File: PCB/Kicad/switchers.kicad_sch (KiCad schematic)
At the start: 44 parts, among them SW1 SWPADL1, SW10 SWPADR2, SW11 SWPADR3, SW12 SWPADR4, SW13 SWPADR5, SW14 SWPADR6, SW15 SWPADR7, SW16 SWPADR8, SW17 SWPLAYL, SW18 SWCUEL, SW19 SWSHIFTL, SW2 SWPADL2, SW20 SWSYNCL, SW21 SWRANGEL, SW22 SWFX1L, SW23 SWFX2L, SW24 SWFX3L, SW25 SWBR-PREVL, SW26 SWBR-BACKL, SW27 SWPLAYR, SW28 SWCUER, SW29 SWSHIFTR, SW3 SWPADL3, SW30 SWSYNCR, SW31 SWRANGER, SW32 SWFX1R, SW33 SWFX2R, SW34 SWFX3R, SW35 SWBR-PREVR, SW36 SWBR-BACKR, SW37 SWPCUEL1, SW38 SWPCUEL2, SW39 SWPCUEL3, SW4 SWPADL4, SW40 SWSEL1, SW41 SWSEL2, SW42 SWSEL3, SW43 BROWSER-L, SW44 BROWSER-R, SW5 SWPADL5, SW6 SWPADL6, SW7 SWPADL7, SW8 SWPADL8, SW9 SWPADR1

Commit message: fixing 3dmodels
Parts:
- SW17, SW18, SW19, SW20, SW21, SW22, SW23, SW24, SW25, SW26, SW27, SW28, SW29, SW30, SW31, SW32, SW33, SW34, SW35, SW36, SW37, SW38, SW39, SW40, SW41, SW42: footprint Button_Switch_THT:SW_PUSH_6mm_H5mm -> Library:SW_PUSH_6mm_H5mm
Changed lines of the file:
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@@
     (property "Reference" "SW17" (id 0) (at 106.68 25.781 0))
     (property "Value" "SWPLAYL" (id 1) (at 106.68 28.0924 0))
-    (property "Footprint" "Button_Switch_THT:SW_PUSH_6mm_H5mm" (id 2) (at 106.68 27.94 0)
+    (property "Footprint" "Library:SW_PUSH_6mm_H5mm" (id 2) (at 106.68 27.94 0)
       (effects (font (size 1.27 1.27)) hide)
     )
@@
     (property "Reference" "SW18" (id 0) (at 106.68 43.561 0))
     (property "Value" "SWCUEL" (id 1) (at 106.68 45.8724 0))
-    (property "Footprint" "Button_Switch_THT:SW_PUSH_6mm_H5mm" (id 2) (at 106.68 45.72 0)
+    (property "Footprint" "Library:SW_PUSH_6mm_H5mm" (id 2) (at 106.68 45.72 0)
       (effects (font (size 1.27 1.27)) hide)
     )
@@
     (property "Reference" "SW19" (id 0) (at 106.68 58.801 0))
     (property "Value" "SWSHIFTL" (id 1) (at 106.68 61.1124 0))
-    (property "Footprint" "Button_Switch_THT:SW_PUSH_6mm_H5mm" (id 2) (at 106.68 60.96 0)
+    (property "Footprint" "Library:SW_PUSH_6mm_H5mm" (id 2) (at 106.68 60.96 0)
       (effects (font (size 1.27 1.27)) hide)
     )
@@
     (property "Reference" "SW20" (id 0) (at 106.68 75.311 0))
     (property "Value" "SWSYNCL" (id 1) (at 106.68 77.6224 0))
-    (property "Footprint" "Button_Switch_THT:SW_PUSH_6mm_H5mm" (id 2) (at 106.68 77.47 0)
+    (property "Footprint" "Library:SW_PUSH_6mm_H5mm" (id 2) (at 106.68 77.47 0)
       (effects (font (size 1.27 1.27)) hide)
     )
@@
     (property "Reference" "SW21" (id 0) (at 106.68 90.551 0))
     (property "Value" "SWRANGEL" (id 1) (at 106.68 92.8624 0))
-    (property "Footprint" "Button_Switch_THT:SW_PUSH_6mm_H5mm" (id 2) (at 106.68 92.71 0)
+    (property "Footprint" "Library:SW_PUSH_6mm_H5mm" (id 2) (at 106.68 92.71 0)
       (effects (font (size 1.27 1.27)) hide)
     )
@@
     (property "Reference" "SW22" (id 0) (at 106.68 107.061 0))
     (property "Value" "SWFX1L" (id 1) (at 106.68 109.3724 0))
-    (property "Footprint" "Button_Switch_THT:SW_PUSH_6mm_H5mm" (id 2) (at 106.68 109.22 0)
+    (property "Footprint" "Library:SW_PUSH_6mm_H5mm" (id 2) (at 106.68 109.22 0)
       (effects (font (size 1.27 1.27)) hide)
     )
@@
     (property "Reference" "SW23" (id 0) (at 106.68 123.571 0))
     (property "Value" "SWFX2L" (id 1) (at 106.68 125.8824 0))
-    (property "Footprint" "Button_Switch_THT:SW_PUSH_6mm_H5mm" (id 2) (at 106.68 125.73 0)
+    (property "Footprint" "Library:SW_PUSH_6mm_H5mm" (id 2) (at 106.68 125.73 0)
       (effects (font (size 1.27 1.27)) hide)
     )
@@
     (property "Reference" "SW24" (id 0) (at 106.68 140.081 0))
     (property "Value" "SWFX3L" (id 1) (at 106.68 142.3924 0))
-    (property "Footprint" "Button_Switch_THT:SW_PUSH_6mm_H5mm" (id 2) (at 106.68 142.24 0)
+    (property "Footprint" "Library:SW_PUSH_6mm_H5mm" (id 2) (at 106.68 142.24 0)
       (effects (font (size 1.27 1.27)) hide)
     )
@@
     (property "Reference" "SW25" (id 0) (at 106.68 160.401 0))
     (property "Value" "SWBR-PREVL" (id 1) (at 106.68 162.7124 0))
-    (property "Footprint" "Button_Switch_THT:SW_PUSH_6mm_H5mm" (id 2) (at 106.68 162.56 0)
+    (property "Footprint" "Library:SW_PUSH_6mm_H5mm" (id 2) (at 106.68 162.56 0)
       (effects (font (size 1.27 1.27)) hide)
     )
@@
     (property "Reference" "SW26" (id 0) (at 106.68 178.181 0))
     (property "Value" "SWBR-BACKL" (id 1) (at 106.68 180.4924 0))
-    (property "Footprint" "Button_Switch_THT:SW_PUSH_6mm_H5mm" (id 2) (at 106.68 180.34 0)
+    (property "Footprint" "Library:SW_PUSH_6mm_H5mm" (id 2) (at 106.68 180.34 0)
       (effects (font (size 1.27 1.27)) hide)
     )
@@
     (property "Reference" "SW27" (id 0) (at 140.97 25.781 0))
     (property "Value" "SWPLAYR" (id 1) (at 140.97 28.0924 0))
-    (property "Footprint" "Button_Switch_THT:SW_PUSH_6mm_H5mm" (id 2) (at 140.97 27.94 0)
+    (property "Footprint" "Library:SW_PUSH_6mm_H5mm" (id 2) (at 140.97 27.94 0)
       (effects (font (size 1.27 1.27)) hide)
     )
@@
     (property "Reference" "SW28" (id 0) (at 140.97 43.561 0))
     (property "Value" "SWCUER" (id 1) (at 140.97 45.8724 0))
-    (property "Footprint" "Button_Switch_THT:SW_PUSH_6mm_H5mm" (id 2) (at 140.97 45.72 0)
+    (property "Footprint" "Library:SW_PUSH_6mm_H5mm" (id 2) (at 140.97 45.72 0)
       (effects (font (size 1.27 1.27)) hide)
     )
@@
     (property "Reference" "SW29" (id 0) (at 140.97 58.801 0))
     (property "Value" "SWSHIFTR" (id 1) (at 140.97 61.1124 0))
-    (property "Footprint" "Button_Switch_THT:SW_PUSH_6mm_H5mm" (id 2) (at 140.97 60.96 0)
+    (property "Footprint" "Library:SW_PUSH_6mm_H5mm" (id 2) (at 140.97 60.96 0)
       (effects (font (size 1.27 1.27)) hide)
     )
@@
     (property "Reference" "SW30" (id 0) (at 140.97 75.311 0))
     (property "Value" "SWSYNCR" (id 1) (at 140.97 77.6224 0))
-    (property "Footprint" "Button_Switch_THT:SW_PUSH_6mm_H5mm" (id 2) (at 140.97 77.47 0)
+    (property "Footprint" "Library:SW_PUSH_6mm_H5mm" (id 2) (at 140.97 77.47 0)
       (effects (font (size 1.27 1.27)) hide)
     )
@@
     (property "Reference" "SW31" (id 0) (at 140.97 90.551 0))
     (property "Value" "SWRANGER" (id 1) (at 140.97 92.8624 0))
-    (property "Footprint" "Button_Switch_THT:SW_PUSH_6mm_H5mm" (id 2) (at 140.97 92.71 0)
+    (property "Footprint" "Library:SW_PUSH_6mm_H5mm" (id 2) (at 140.97 92.71 0)
       (effects (font (size 1.27 1.27)) hide)
     )
@@
     (property "Reference" "SW32" (id 0) (at 140.97 107.061 0))
     (property "Value" "SWFX1R" (id 1) (at 140.97 109.3724 0))
-    (property "Footprint" "Button_Switch_THT:SW_PUSH_6mm_H5mm" (id 2) (at 140.97 109.22 0)
+    (property "Footprint" "Library:SW_PUSH_6mm_H5mm" (id 2) (at 140.97 109.22 0)
       (effects (font (size 1.27 1.27)) hide)
     )
@@
     (property "Reference" "SW33" (id 0) (at 140.97 123.571 0))
     (property "Value" "SWFX2R" (id 1) (at 140.97 125.8824 0))
-    (property "Footprint" "Button_Switch_THT:SW_PUSH_6mm_H5mm" (id 2) (at 140.97 125.73 0)
+    (property "Footprint" "Library:SW_PUSH_6mm_H5mm" (id 2) (at 140.97 125.73 0)
       (effects (font (size 1.27 1.27)) hide)
     )
@@
     (property "Reference" "SW34" (id 0) (at 140.97 140.081 0))
     (property "Value" "SWFX3R" (id 1) (at 140.97 142.3924 0))
-    (property "Footprint" "Button_Switch_THT:SW_PUSH_6mm_H5mm" (id 2) (at 140.97 142.24 0)
+    (property "Footprint" "Library:SW_PUSH_6mm_H5mm" (id 2) (at 140.97 142.24 0)
       (effects (font (size 1.27 1.27)) hide)
     )
@@
     (property "Reference" "SW35" (id 0) (at 143.51 160.401 0))
     (property "Value" "SWBR-PREVR" (id 1) (at 143.51 162.7124 0))
-    (property "Footprint" "Button_Switch_THT:SW_PUSH_6mm_H5mm" (id 2) (at 143.51 162.56 0)
+    (property "Footprint" "Library:SW_PUSH_6mm_H5mm" (id 2) (at 143.51 162.56 0)
       (effects (font (size 1.27 1.27)) hide)
     )
@@
     (property "Reference" "SW36" (id 0) (at 143.51 178.181 0))
     (property "Value" "SWBR-BACKR" (id 1) (at 143.51 180.4924 0))
-    (property "Footprint" "Button_Switch_THT:SW_PUSH_6mm_H5mm" (id 2) (at 143.51 180.34 0)
+    (property "Footprint" "Library:SW_PUSH_6mm_H5mm" (id 2) (at 143.51 180.34 0)
       (effects (font (size 1.27 1.27)) hide)
     )
@@
     (property "Reference" "SW37" (id 0) (at 173.99 25.781 0))
     (property "Value" "SWPCUEL1" (id 1) (at 173.99 28.0924 0))
-    (property "Footprint" "Button_Switch_THT:SW_PUSH_6mm_H5mm" (id 2) (at 173.99 27.94 0)
+    (property "Footprint" "Library:SW_PUSH_6mm_H5mm" (id 2) (at 173.99 27.94 0)
       (effects (font (size 1.27 1.27)) hide)
     )
@@
     (property "Reference" "SW38" (id 0) (at 173.99 43.561 0))
     (property "Value" "SWPCUEL2" (id 1) (at 173.99 45.8724 0))
-    (property "Footprint" "Button_Switch_THT:SW_PUSH_6mm_H5mm" (id 2) (at 173.99 45.72 0)
+    (property "Footprint" "Library:SW_PUSH_6mm_H5mm" (id 2) (at 173.99 45.72 0)
       (effects (font (size 1.27 1.27)) hide)
     )
@@
     (property "Reference" "SW39" (id 0) (at 173.99 58.801 0))
     (property "Value" "SWPCUEL3" (id 1) (at 173.99 61.1124 0))
-    (property "Footprint" "Button_Switch_THT:SW_PUSH_6mm_H5mm" (id 2) (at 173.99 60.96 0)
+    (property "Footprint" "Library:SW_PUSH_6mm_H5mm" (id 2) (at 173.99 60.96 0)
       (effects (font (size 1.27 1.27)) hide)
     )
@@
     (property "Reference" "SW40" (id 0) (at 173.99 75.311 0))
     (property "Value" "SWSEL1" (id 1) (at 173.99 77.6224 0))
-    (property "Footprint" "Button_Switch_THT:SW_PUSH_6mm_H5mm" (id 2) (at 173.99 77.47 0)
+    (property "Footprint" "Library:SW_PUSH_6mm_H5mm" (id 2) (at 173.99 77.47 0)
       (effects (font (size 1.27 1.27)) hide)
     )
@@
     (property "Reference" "SW41" (id 0) (at 173.99 90.551 0))
     (property "Value" "SWSEL2" (id 1) (at 173.99 92.8624 0))
-    (property "Footprint" "Button_Switch_THT:SW_PUSH_6mm_H5mm" (id 2) (at 173.99 92.71 0)
+    (property "Footprint" "Library:SW_PUSH_6mm_H5mm" (id 2) (at 173.99 92.71 0)
       (effects (font (size 1.27 1.27)) hide)
     )
@@
     (property "Reference" "SW42" (id 0) (at 173.99 107.061 0))
     (property "Value" "SWSEL3" (id 1) (at 173.99 109.3724 0))
-    (property "Footprint" "Button_Switch_THT:SW_PUSH_6mm_H5mm" (id 2) (at 173.99 109.22 0)
-      (effects (font (size 1.27 1.27)) hide)
-    )
+    (property "Footprint" "Library:SW_PUSH_6mm_H5mm" (id 2) (at 173.99 109.22 0)
+      (effects (font (size 1.27 1.27)) hide)
+    )

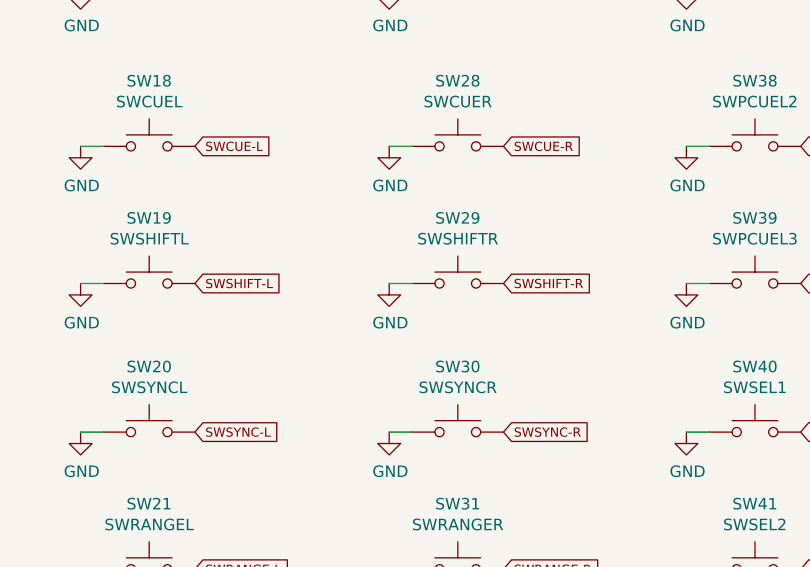
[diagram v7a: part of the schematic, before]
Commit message: change few pins  and programming
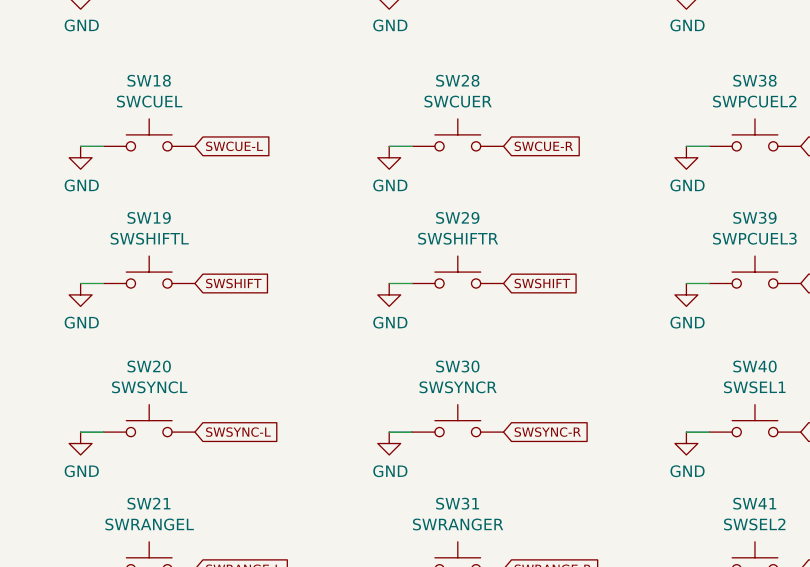
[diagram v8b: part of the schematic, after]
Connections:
- net SWSHIFT-R is gone; now on net SWSHIFT: SW29.2
- net SWSHIFT-L renamed SWSHIFT
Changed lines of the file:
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@@
     )
   )
-  (global_label "SWSHIFT-L" (shape input) (at 111.76 66.04 0)
+  (global_label "SWSHIFT" (shape input) (at 111.76 66.04 0)
     (effects (font (size 1.016 1.016)) (justify left))
-    (property "Intersheet References" "${INTERSHEET_REFS}" (id 0) (at 0 0 0)
-      (effects (font (size 1.27 1.27)) hide)
+    (property "Intersheet References" "${INTERSHEET_REFS}" (id 0) (at 119.9799 65.9765 0)
+      (effects (font (size 1.016 1.016)) (justify left) hide)
     )
   )
@@
     )
   )
-  (global_label "SWSHIFT-R" (shape input) (at 146.05 66.04 0)
+  (global_label "SWSHIFT" (shape input) (at 146.05 66.04 0)
     (effects (font (size 1.016 1.016)) (justify left))
-    (property "Intersheet References" "${INTERSHEET_REFS}" (id 0) (at 0 0 0)
-      (effects (font (size 1.27 1.27)) hide)
+    (property "Intersheet References" "${INTERSHEET_REFS}" (id 0) (at 154.2699 65.9765 0)
+      (effects (font (size 1.016 1.016)) (justify left) hide)
     )
   )
